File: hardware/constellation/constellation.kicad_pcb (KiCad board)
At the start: 2 copper layers, 395.2 x 272.1 mm, 122 parts

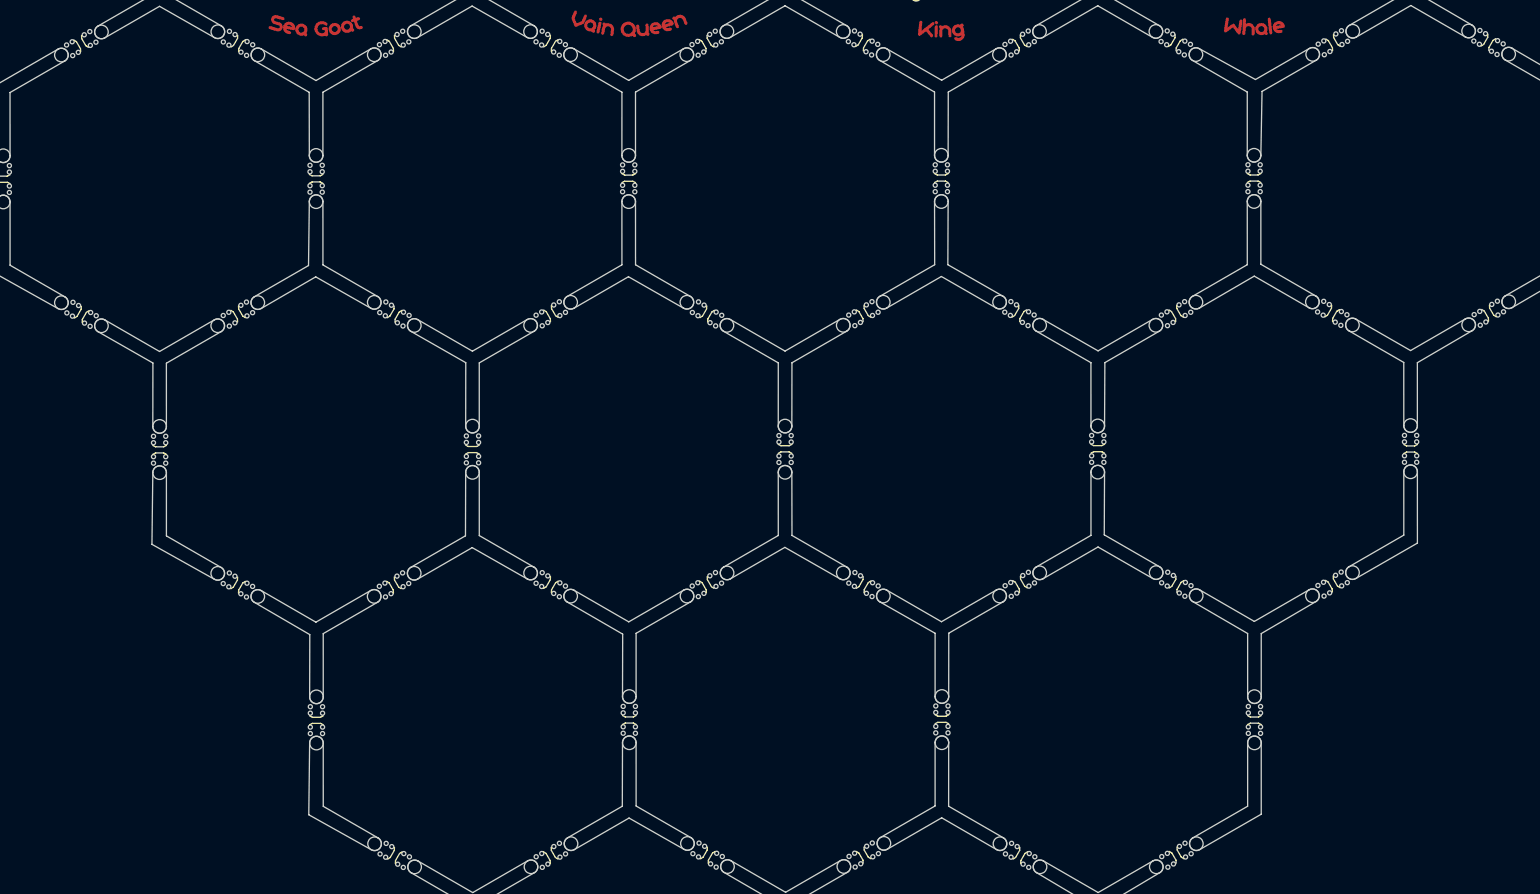
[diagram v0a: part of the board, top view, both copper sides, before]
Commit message: Added the rest of the constellations
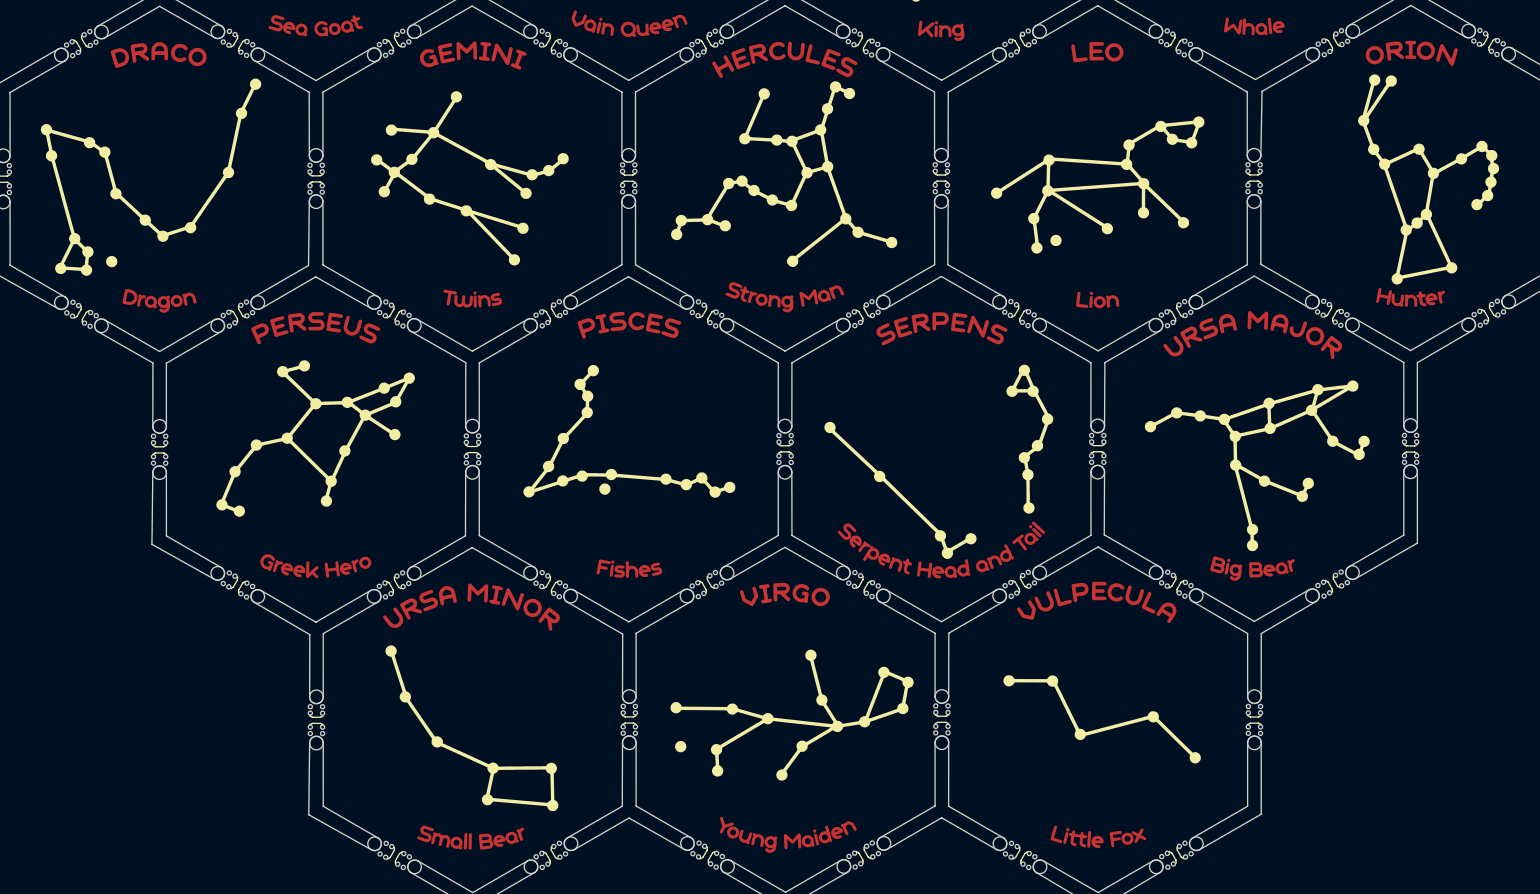
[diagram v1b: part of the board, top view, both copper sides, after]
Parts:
- added ? (x4): , Graphics, F.Cu at (143.2, 157.4)
- added ?: , Graphics, B.Cu at (51.0, 157.3)
- added ?: , Graphics, B.Cu at (120.1, 117.6)
- added ?: , Graphics, B.Cu at (74.1, 117.5)
- added ?: , Graphics, B.Cu at (189.2, 157.3)
- added ?: , Graphics, B.Cu at (74.1, 197.3)
- added ?: , Graphics, B.Cu at (143.1, 157.3)
- added ?: , Graphics, B.Cu at (97.1, 157.4)
- added ? (x4): , Graphics, F.Cu at (74.1, 117.5)
- added ? (x3): , Graphics, F.Cu at (120.2, 197.2)
- added ? (x4): , Graphics, F.Cu at (189.1, 157.2)
- added ? (x4): , Graphics, F.Cu at (120.1, 117.6)
- added ? (x4): , Graphics, F.Cu at (166.2, 197.1)
- added ? (x4): , Graphics, F.Cu at (166.1, 117.6)
- added ? (x4): , Graphics, F.Cu at (51.0, 157.3)
- added ? (x4): , Graphics, F.Cu at (212.3, 117.4)
- added ? (x4): , Graphics, F.Cu at (74.1, 197.3)
- added ? (x3): , Graphics, F.Cu at (97.2, 157.3)
- added ?: , Graphics, F.Cu at (189.2, 157.3)
- added ? (x4): , Graphics, F.Cu at (28.1, 117.6)
- added ?: , Graphics, F.Cu at (143.2, 157.3)
- added ?: , Graphics, F.Cu at (143.1, 157.3)
- added ?: , Graphics, F.Cu at (97.1, 157.4)
- added ?: , Graphics, B.Cu at (166.2, 197.1)
- added ?: , Graphics, B.Cu at (28.1, 117.6)
- added ?: , Graphics, B.Cu at (212.3, 117.4)
- added ?: , Graphics, B.Cu at (189.1, 157.2)
- added ?: , Graphics, B.Cu at (166.1, 117.6)
- added ?: , Graphics, B.Cu at (143.2, 157.3)
- added ?: , Graphics, B.Cu at (143.2, 157.4)

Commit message: Added order number and tooling holes
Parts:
- removed the mouse-bite-2mm-slot at (202.3, 246.5)
- removed the mouse-bite-2mm-slot at (110.2, 246.6)
- removed the mouse-bite-2mm-slot at (52.7, 107.3)
- removed the mouse-bite-2mm-slot at (41.2, 167.0)
- removed the mouse-bite-2mm-slot at (29.6, 147.1)
- removed the mouse-bite-2mm-slot at (236.8, 107.0)
- removed the mouse-bite-2mm-slot at (213.8, 226.7)
- removed the mouse-bite-2mm-slot at (64.1, 87.3)
- removed the mouse-bite-2mm-slot at (248.1, 126.9)
- removed the mouse-bite-2mm-slot at (52.6, 187.0)
- removed the mouse-bite-2mm-slot at (156.2, 246.6)
- removed the mouse-bite-2mm-slot at (87.3, 246.6)
- removed the mouse-bite-2mm-slot at (236.7, 186.8)
- removed the mouse-bite-2mm-slot at (110.1, 47.3)
- removed the mouse-bite-2mm-slot at (248.3, 166.8)
- removed the mouse-bite-2mm-slot at (75.7, 226.8)
- removed the mouse-bite-2mm-slot at (87.1, 47.5)
- removed the mouse-bite-2mm-slot at (133.3, 246.6)
- removed the mouse-bite-2mm-slot at (259.7, 146.8)
- removed the mouse-bite-2mm-slot at (133.2, 47.4)
- removed the mouse-bite-2mm-slot at (202.2, 47.3)
- removed the mouse-bite-2mm-slot at (225.2, 87.1)
- removed the mouse-bite-2mm-slot at (179.3, 47.3)
- removed the mouse-bite-2mm-slot at (41.0, 127.2)
- removed the mouse-bite-2mm-slot at (64.2, 206.8)
- removed the mouse-bite-2mm-slot at (225.3, 206.6)
- removed the mouse-bite-2mm-slot at (156.1, 47.3)
- removed the mouse-bite-2mm-slot at (179.3, 246.6)
- removed the mouse-bite-2mm-slot at (213.8, 67.2)
- removed the mouse-bite-2mm-slot at (75.7, 67.4)
- added REF**: Fiducial_1mm_Mask2mm, Fiducial:Fiducial_1mm_Mask2mm, F.Cu at (5.00, 20.0)
- added REF**: Fiducial_1mm_Mask2mm, Fiducial:Fiducial_1mm_Mask2mm, F.Cu at (237.0, 204.0)
- added REF**: MountingHole_2mm, MountingHole:MountingHole_2mm, F.Cu at (237.0, 5.00)
- added REF**: MountingHole_2mm, MountingHole:MountingHole_2mm, F.Cu at (237.0, 219.0)
- added REF**: MountingHole_2mm, MountingHole:MountingHole_2mm, F.Cu at (5.00, 219.0)
- added REF**: Fiducial_1mm_Mask2mm, Fiducial:Fiducial_1mm_Mask2mm, F.Cu at (222.0, 5.00)
- added REF**: Fiducial_1mm_Mask2mm, Fiducial:Fiducial_1mm_Mask2mm, F.Cu at (20.0, 219.0)
- added REF**: MountingHole_2mm, MountingHole:MountingHole_2mm, F.Cu at (5.00, 5.00)
- added mouse-bite-2mm-slot: VAL**, SWS-Library:mouse-bite-2mm-slot_edge, F.Cu at (40.5, 52.6)
- added mouse-bite-2mm-slot: VAL**, SWS-Library:mouse-bite-2mm-slot_edge, F.Cu at (155.8, 212.0)
- added mouse-bite-2mm-slot: VAL**, SWS-Library:mouse-bite-2mm-slot_edge, F.Cu at (201.6, 52.5)
- added mouse-bite-2mm-slot: VAL**, SWS-Library:mouse-bite-2mm-slot_edge, F.Cu at (86.5, 12.7)
- added mouse-bite-2mm-slot: VAL**, SWS-Library:mouse-bite-2mm-slot_edge, F.Cu at (29.1, 152.3)
- added mouse-bite-2mm-slot: VAL**, SWS-Library:mouse-bite-2mm-slot_edge, F.Cu at (224.6, 92.3)
- added mouse-bite-2mm-slot: VAL**, SWS-Library:mouse-bite-2mm-slot_edge, F.Cu at (29.1, 72.6)
- added mouse-bite-2mm-slot: VAL**, SWS-Library:mouse-bite-2mm-slot_edge, F.Cu at (52.2, 192.1)
- added mouse-bite-2mm-slot: VAL**, SWS-Library:mouse-bite-2mm-slot_edge, F.Cu at (190.2, 191.8)
- added mouse-bite-2mm-slot: VAL**, SWS-Library:mouse-bite-2mm-slot_edge, F.Cu at (86.8, 211.9)
- added mouse-bite-2mm-slot: VAL**, SWS-Library:mouse-bite-2mm-slot_edge, F.Cu at (40.7, 172.2)
- added mouse-bite-2mm-slot: VAL**, SWS-Library:mouse-bite-2mm-slot_edge, F.Cu at (201.8, 172.0)
- added mouse-bite-2mm-slot: VAL**, SWS-Library:mouse-bite-2mm-slot_edge, F.Cu at (213.2, 152.0)
- added mouse-bite-2mm-slot: VAL**, SWS-Library:mouse-bite-2mm-slot_edge, F.Cu at (109.8, 211.9)
- added mouse-bite-2mm-slot: VAL**, SWS-Library:mouse-bite-2mm-slot_edge, F.Cu at (155.6, 12.8)
- added mouse-bite-2mm-slot: VAL**, SWS-Library:mouse-bite-2mm-slot_edge, F.Cu at (63.5, 12.8)
- added mouse-bite-2mm-slot: VAL**, SWS-Library:mouse-bite-2mm-slot_edge, F.Cu at (52.1, 32.6)
- added mouse-bite-2mm-slot: VAL**, SWS-Library:mouse-bite-2mm-slot_edge, F.Cu at (17.7, 132.4)
- added mouse-bite-2mm-slot: VAL**, SWS-Library:mouse-bite-2mm-slot_edge, F.Cu at (224.8, 132.1)
- added mouse-bite-2mm-slot: VAL**, SWS-Library:mouse-bite-2mm-slot_edge, F.Cu at (109.5, 12.8)
- added mouse-bite-2mm-slot: VAL**, SWS-Library:mouse-bite-2mm-slot_edge, F.Cu at (178.8, 211.9)
- added mouse-bite-2mm-slot: VAL**, SWS-Library:mouse-bite-2mm-slot_edge, F.Cu at (63.8, 212.0)
- added mouse-bite-2mm-slot: VAL**, SWS-Library:mouse-bite-2mm-slot_edge, F.Cu at (213.3, 72.3)
- added mouse-bite-2mm-slot: VAL**, SWS-Library:mouse-bite-2mm-slot_edge, F.Cu at (178.6, 12.6)
- added mouse-bite-2mm-slot: VAL**, SWS-Library:mouse-bite-2mm-slot_edge, F.Cu at (132.6, 12.7)
- added mouse-bite-2mm-slot: VAL**, SWS-Library:mouse-bite-2mm-slot_edge, F.Cu at (17.5, 92.5)
- added mouse-bite-2mm-slot: VAL**, SWS-Library:mouse-bite-2mm-slot_edge, F.Cu at (132.8, 211.8)
- added mouse-bite-2mm-slot: VAL**, SWS-Library:mouse-bite-2mm-slot_edge, F.Cu at (190.2, 32.5)
- moved ? 41.9 mm to (73.6, 43.0) (x5)
- moved mouse-bite-2mm-slot 41.9 mm to (86.7, 92.5)
- moved mouse-bite-2mm-slot 41.9 mm to (155.6, 52.5)
- moved ? 41.9 mm to (27.5, 43.0) (x5)
- moved mouse-bite-2mm-slot 41.9 mm to (109.6, 52.5)
- moved mouse-bite-2mm-slot 41.9 mm to (132.8, 172.1)
- moved ? 41.9 mm to (142.7, 162.4)
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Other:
- board size 395.2 x 272.1 mm -> 242 x 224 mm
- board text added: "JLCJLCJLCJLC"

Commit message: Roughly placed all the LEDs
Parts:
- added TP266: TestPoint, TestPoint:TestPoint_Pad_D1.5mm, F.Cu at (2.58, 25.7)
- added TP267: TestPoint, TestPoint:TestPoint_Pad_D1.5mm, F.Cu at (2.41, 29.8)
- added TP268: TestPoint, TestPoint:TestPoint_Pad_D1.5mm, F.Cu at (2.41, 33.3)
- added U1: XL-1010RGBC, easyeda2kicad:LED-SMD_4P-L1.0-W1.0-TL_XL-1010RGBC-WS2812B, F.Cu at (65.5, 21.0)
- added U10: XL-1010RGBC, easyeda2kicad:LED-SMD_4P-L1.0-W1.0-TL_XL-1010RGBC-WS2812B, F.Cu at (74.1, 40.8)
- added U100: XL-1010RGBC, easyeda2kicad:LED-SMD_4P-L1.0-W1.0-TL_XL-1010RGBC-WS2812B, F.Cu at (22.1, 124.6)
- added U101: XL-1010RGBC, easyeda2kicad:LED-SMD_4P-L1.0-W1.0-TL_XL-1010RGBC-WS2812B, F.Cu at (61.1, 109.6)
- added U102: XL-1010RGBC, easyeda2kicad:LED-SMD_4P-L1.0-W1.0-TL_XL-1010RGBC-WS2812B, F.Cu at (62.2, 114.3)
- added U103: XL-1010RGBC, easyeda2kicad:LED-SMD_4P-L1.0-W1.0-TL_XL-1010RGBC-WS2812B, F.Cu at (63.6, 111.4)
- added U104: XL-1010RGBC, easyeda2kicad:LED-SMD_4P-L1.0-W1.0-TL_XL-1010RGBC-WS2812B, F.Cu at (66.2, 109.5)
- added U105: XL-1010RGBC, easyeda2kicad:LED-SMD_4P-L1.0-W1.0-TL_XL-1010RGBC-WS2812B, F.Cu at (68.9, 115.4)
- added U106: XL-1010RGBC, easyeda2kicad:LED-SMD_4P-L1.0-W1.0-TL_XL-1010RGBC-WS2812B, F.Cu at (74.2, 117.1)
- added U107: XL-1010RGBC, easyeda2kicad:LED-SMD_4P-L1.0-W1.0-TL_XL-1010RGBC-WS2812B, F.Cu at (81.3, 124.3)
- added U108: XL-1010RGBC, easyeda2kicad:LED-SMD_4P-L1.0-W1.0-TL_XL-1010RGBC-WS2812B, F.Cu at (82.6, 119.7)
- added U109: XL-1010RGBC, easyeda2kicad:LED-SMD_4P-L1.0-W1.0-TL_XL-1010RGBC-WS2812B, F.Cu at (63.2, 105.1)
- added U11: XL-1010RGBC, easyeda2kicad:LED-SMD_4P-L1.0-W1.0-TL_XL-1010RGBC-WS2812B, F.Cu at (74.3, 38.5)
- added U110: XL-1010RGBC, easyeda2kicad:LED-SMD_4P-L1.0-W1.0-TL_XL-1010RGBC-WS2812B, F.Cu at (69.4, 105.6)
- added U111: XL-1010RGBC, easyeda2kicad:LED-SMD_4P-L1.0-W1.0-TL_XL-1010RGBC-WS2812B, F.Cu at (72.8, 100.3)
- added U112: XL-1010RGBC, easyeda2kicad:LED-SMD_4P-L1.0-W1.0-TL_XL-1010RGBC-WS2812B, F.Cu at (77.8, 110.3)
- added U113: XL-1010RGBC, easyeda2kicad:LED-SMD_4P-L1.0-W1.0-TL_XL-1010RGBC-WS2812B, F.Cu at (83.1, 114.5)
- added U114: XL-1010RGBC, easyeda2kicad:LED-SMD_4P-L1.0-W1.0-TL_XL-1010RGBC-WS2812B, F.Cu at (83.9, 111.8)
- added U115: XL-1010RGBC, easyeda2kicad:LED-SMD_4P-L1.0-W1.0-TL_XL-1010RGBC-WS2812B, F.Cu at (86.3, 111.2)
- added U116: XL-1010RGBC, easyeda2kicad:LED-SMD_4P-L1.0-W1.0-TL_XL-1010RGBC-WS2812B, F.Cu at (88.5, 109.4)
- added U117: XL-1010RGBC, easyeda2kicad:LED-SMD_4P-L1.0-W1.0-TL_XL-1010RGBC-WS2812B, F.Cu at (105.2, 120.6)
- added U118: XL-1010RGBC, easyeda2kicad:LED-SMD_4P-L1.0-W1.0-TL_XL-1010RGBC-WS2812B, F.Cu at (105.9, 118.4)
- added U119: XL-1010RGBC, easyeda2kicad:LED-SMD_4P-L1.0-W1.0-TL_XL-1010RGBC-WS2812B, F.Cu at (109.7, 118.4)
- added U12: XL-1010RGBC, easyeda2kicad:LED-SMD_4P-L1.0-W1.0-TL_XL-1010RGBC-WS2812B, F.Cu at (74.6, 36.1)
- added U120: XL-1010RGBC, easyeda2kicad:LED-SMD_4P-L1.0-W1.0-TL_XL-1010RGBC-WS2812B, F.Cu at (112.4, 119.3)
- added U121: XL-1010RGBC, easyeda2kicad:LED-SMD_4P-L1.0-W1.0-TL_XL-1010RGBC-WS2812B, F.Cu at (112.8, 113.1)
- added U122: XL-1010RGBC, easyeda2kicad:LED-SMD_4P-L1.0-W1.0-TL_XL-1010RGBC-WS2812B, F.Cu at (114.9, 112.7)
- added U123: XL-1010RGBC, easyeda2kicad:LED-SMD_4P-L1.0-W1.0-TL_XL-1010RGBC-WS2812B, F.Cu at (116.6, 114.1)
- added U124: XL-1010RGBC, easyeda2kicad:LED-SMD_4P-L1.0-W1.0-TL_XL-1010RGBC-WS2812B, F.Cu at (119.3, 115.5)
- added U125: XL-1010RGBC, easyeda2kicad:LED-SMD_4P-L1.0-W1.0-TL_XL-1010RGBC-WS2812B, F.Cu at (122.1, 116.3)
- added U126: XL-1010RGBC, easyeda2kicad:LED-SMD_4P-L1.0-W1.0-TL_XL-1010RGBC-WS2812B, F.Cu at (124.4, 111.5)
- added U127: XL-1010RGBC, easyeda2kicad:LED-SMD_4P-L1.0-W1.0-TL_XL-1010RGBC-WS2812B, F.Cu at (122.2, 106.8)
- added U128: XL-1010RGBC, easyeda2kicad:LED-SMD_4P-L1.0-W1.0-TL_XL-1010RGBC-WS2812B, F.Cu at (119.9, 106.7)
- added U129: XL-1010RGBC, easyeda2kicad:LED-SMD_4P-L1.0-W1.0-TL_XL-1010RGBC-WS2812B, F.Cu at (115.2, 106.5)
- added U13: XL-1010RGBC, easyeda2kicad:LED-SMD_4P-L1.0-W1.0-TL_XL-1010RGBC-WS2812B, F.Cu at (78.5, 33.6)
- added U130: XL-1010RGBC, easyeda2kicad:LED-SMD_4P-L1.0-W1.0-TL_XL-1010RGBC-WS2812B, F.Cu at (118.1, 99.9)
- added U131: XL-1010RGBC, easyeda2kicad:LED-SMD_4P-L1.0-W1.0-TL_XL-1010RGBC-WS2812B, F.Cu at (130.7, 99.8)
- added U132: XL-1010RGBC, easyeda2kicad:LED-SMD_4P-L1.0-W1.0-TL_XL-1010RGBC-WS2812B, F.Cu at (128.6, 98.9)
- added U133: XL-1010RGBC, easyeda2kicad:LED-SMD_4P-L1.0-W1.0-TL_XL-1010RGBC-WS2812B, F.Cu at (127.4, 102.1)
- added U134: XL-1010RGBC, easyeda2kicad:LED-SMD_4P-L1.0-W1.0-TL_XL-1010RGBC-WS2812B, F.Cu at (126.4, 105.2)
- added U135: XL-1010RGBC, easyeda2kicad:LED-SMD_4P-L1.0-W1.0-TL_XL-1010RGBC-WS2812B, F.Cu at (127.3, 110.6)
- added U136: XL-1010RGBC, easyeda2kicad:LED-SMD_4P-L1.0-W1.0-TL_XL-1010RGBC-WS2812B, F.Cu at (130.1, 118.2)
- added U137: XL-1010RGBC, easyeda2kicad:LED-SMD_4P-L1.0-W1.0-TL_XL-1010RGBC-WS2812B, F.Cu at (122.3, 124.5)
- added U138: XL-1010RGBC, easyeda2kicad:LED-SMD_4P-L1.0-W1.0-TL_XL-1010RGBC-WS2812B, F.Cu at (131.9, 120.2)
- added U139: XL-1010RGBC, easyeda2kicad:LED-SMD_4P-L1.0-W1.0-TL_XL-1010RGBC-WS2812B, F.Cu at (136.8, 121.8)
- added U14: XL-1010RGBC, easyeda2kicad:LED-SMD_4P-L1.0-W1.0-TL_XL-1010RGBC-WS2812B, F.Cu at (78.6, 31.1)
- added U140: XL-1010RGBC, easyeda2kicad:LED-SMD_4P-L1.0-W1.0-TL_XL-1010RGBC-WS2812B, F.Cu at (152.3, 114.5)
- added U141: XL-1010RGBC, easyeda2kicad:LED-SMD_4P-L1.0-W1.0-TL_XL-1010RGBC-WS2812B, F.Cu at (160.0, 109.6)
- added U142: XL-1010RGBC, easyeda2kicad:LED-SMD_4P-L1.0-W1.0-TL_XL-1010RGBC-WS2812B, F.Cu at (159.8, 114.2)
- added U143: XL-1010RGBC, easyeda2kicad:LED-SMD_4P-L1.0-W1.0-TL_XL-1010RGBC-WS2812B, F.Cu at (157.8, 118.3)
- added U144: XL-1010RGBC, easyeda2kicad:LED-SMD_4P-L1.0-W1.0-TL_XL-1010RGBC-WS2812B, F.Cu at (158.2, 122.6)
- added U145: XL-1010RGBC, easyeda2kicad:LED-SMD_4P-L1.0-W1.0-TL_XL-1010RGBC-WS2812B, F.Cu at (161.0, 121.5)
- added U146: XL-1010RGBC, easyeda2kicad:LED-SMD_4P-L1.0-W1.0-TL_XL-1010RGBC-WS2812B, F.Cu at (168.6, 119.7)
- added U147: XL-1010RGBC, easyeda2kicad:LED-SMD_4P-L1.0-W1.0-TL_XL-1010RGBC-WS2812B, F.Cu at (173.9, 117.4)
- added U148: XL-1010RGBC, easyeda2kicad:LED-SMD_4P-L1.0-W1.0-TL_XL-1010RGBC-WS2812B, F.Cu at (179.8, 118.9)
- added U149: XL-1010RGBC, easyeda2kicad:LED-SMD_4P-L1.0-W1.0-TL_XL-1010RGBC-WS2812B, F.Cu at (173.9, 113.1)
- added U15: XL-1010RGBC, easyeda2kicad:LED-SMD_4P-L1.0-W1.0-TL_XL-1010RGBC-WS2812B, F.Cu at (84.7, 25.7)
- added U150: XL-1010RGBC, easyeda2kicad:LED-SMD_4P-L1.0-W1.0-TL_XL-1010RGBC-WS2812B, F.Cu at (171.4, 110.2)
- added U151: XL-1010RGBC, easyeda2kicad:LED-SMD_4P-L1.0-W1.0-TL_XL-1010RGBC-WS2812B, F.Cu at (171.7, 107.4)
- added U152: XL-1010RGBC, easyeda2kicad:LED-SMD_4P-L1.0-W1.0-TL_XL-1010RGBC-WS2812B, F.Cu at (176.4, 104.7)
- added U153: XL-1010RGBC, easyeda2kicad:LED-SMD_4P-L1.0-W1.0-TL_XL-1010RGBC-WS2812B, F.Cu at (178.1, 106.6)
- added U154: XL-1010RGBC, easyeda2kicad:LED-SMD_4P-L1.0-W1.0-TL_XL-1010RGBC-WS2812B, F.Cu at (181.0, 107.1)
- added U155: XL-1010RGBC, easyeda2kicad:LED-SMD_4P-L1.0-W1.0-TL_XL-1010RGBC-WS2812B, F.Cu at (182.0, 104.0)
- added U156: XL-1010RGBC, easyeda2kicad:LED-SMD_4P-L1.0-W1.0-TL_XL-1010RGBC-WS2812B, F.Cu at (207.9, 97.8)
- added U157: XL-1010RGBC, easyeda2kicad:LED-SMD_4P-L1.0-W1.0-TL_XL-1010RGBC-WS2812B, F.Cu at (210.4, 98.0)
- added U158: XL-1010RGBC, easyeda2kicad:LED-SMD_4P-L1.0-W1.0-TL_XL-1010RGBC-WS2812B, F.Cu at (206.3, 103.8)
- added U159: XL-1010RGBC, easyeda2kicad:LED-SMD_4P-L1.0-W1.0-TL_XL-1010RGBC-WS2812B, F.Cu at (207.8, 108.0)
- added U16: XL-1010RGBC, easyeda2kicad:LED-SMD_4P-L1.0-W1.0-TL_XL-1010RGBC-WS2812B, F.Cu at (91.5, 26.6)
- added U160: XL-1010RGBC, easyeda2kicad:LED-SMD_4P-L1.0-W1.0-TL_XL-1010RGBC-WS2812B, F.Cu at (209.4, 110.2)
- added U161: XL-1010RGBC, easyeda2kicad:LED-SMD_4P-L1.0-W1.0-TL_XL-1010RGBC-WS2812B, F.Cu at (212.5, 119.9)
- added U162: XL-1010RGBC, easyeda2kicad:LED-SMD_4P-L1.0-W1.0-TL_XL-1010RGBC-WS2812B, F.Cu at (214.2, 118.8)
- added U163: XL-1010RGBC, easyeda2kicad:LED-SMD_4P-L1.0-W1.0-TL_XL-1010RGBC-WS2812B, F.Cu at (215.7, 117.5)
- added U164: XL-1010RGBC, easyeda2kicad:LED-SMD_4P-L1.0-W1.0-TL_XL-1010RGBC-WS2812B, F.Cu at (216.5, 111.5)
- added U165: XL-1010RGBC, easyeda2kicad:LED-SMD_4P-L1.0-W1.0-TL_XL-1010RGBC-WS2812B, F.Cu at (214.4, 108.0)
- added U166: XL-1010RGBC, easyeda2kicad:LED-SMD_4P-L1.0-W1.0-TL_XL-1010RGBC-WS2812B, F.Cu at (220.7, 109.4)
- added U167: XL-1010RGBC, easyeda2kicad:LED-SMD_4P-L1.0-W1.0-TL_XL-1010RGBC-WS2812B, F.Cu at (223.6, 107.5)
- added U168: XL-1010RGBC, easyeda2kicad:LED-SMD_4P-L1.0-W1.0-TL_XL-1010RGBC-WS2812B, F.Cu at (225.4, 108.8)
- added U169: XL-1010RGBC, easyeda2kicad:LED-SMD_4P-L1.0-W1.0-TL_XL-1010RGBC-WS2812B, F.Cu at (225.5, 110.9)
- added U17: XL-1010RGBC, easyeda2kicad:LED-SMD_4P-L1.0-W1.0-TL_XL-1010RGBC-WS2812B, F.Cu at (80.6, 40.7)
- added U170: XL-1010RGBC, easyeda2kicad:LED-SMD_4P-L1.0-W1.0-TL_XL-1010RGBC-WS2812B, F.Cu at (225.1, 112.9)
- added U171: XL-1010RGBC, easyeda2kicad:LED-SMD_4P-L1.0-W1.0-TL_XL-1010RGBC-WS2812B, F.Cu at (224.6, 114.9)
- added U172: XL-1010RGBC, easyeda2kicad:LED-SMD_4P-L1.0-W1.0-TL_XL-1010RGBC-WS2812B, F.Cu at (222.8, 116.3)
- added U173: XL-1010RGBC, easyeda2kicad:LED-SMD_4P-L1.0-W1.0-TL_XL-1010RGBC-WS2812B, F.Cu at (219.3, 125.5)
- added U174: XL-1010RGBC, easyeda2kicad:LED-SMD_4P-L1.0-W1.0-TL_XL-1010RGBC-WS2812B, F.Cu at (211.2, 127.1)
- added U175: XL-1010RGBC, easyeda2kicad:LED-SMD_4P-L1.0-W1.0-TL_XL-1010RGBC-WS2812B, F.Cu at (204.7, 142.9)
- added U176: XL-1010RGBC, easyeda2kicad:LED-SMD_4P-L1.0-W1.0-TL_XL-1010RGBC-WS2812B, F.Cu at (199.5, 143.5)
- added U177: XL-1010RGBC, easyeda2kicad:LED-SMD_4P-L1.0-W1.0-TL_XL-1010RGBC-WS2812B, F.Cu at (192.4, 145.4)
- added U178: XL-1010RGBC, easyeda2kicad:LED-SMD_4P-L1.0-W1.0-TL_XL-1010RGBC-WS2812B, F.Cu at (185.8, 147.8)
- added U179: XL-1010RGBC, easyeda2kicad:LED-SMD_4P-L1.0-W1.0-TL_XL-1010RGBC-WS2812B, F.Cu at (187.4, 150.3)
- added U18: XL-1010RGBC, easyeda2kicad:LED-SMD_4P-L1.0-W1.0-TL_XL-1010RGBC-WS2812B, F.Cu at (107.4, 37.4)
- added U180: XL-1010RGBC, easyeda2kicad:LED-SMD_4P-L1.0-W1.0-TL_XL-1010RGBC-WS2812B, F.Cu at (192.5, 149.1)
- added U181: XL-1010RGBC, easyeda2kicad:LED-SMD_4P-L1.0-W1.0-TL_XL-1010RGBC-WS2812B, F.Cu at (198.7, 146.5)
- added U182: XL-1010RGBC, easyeda2kicad:LED-SMD_4P-L1.0-W1.0-TL_XL-1010RGBC-WS2812B, F.Cu at (201.8, 151.0)
- added U183: XL-1010RGBC, easyeda2kicad:LED-SMD_4P-L1.0-W1.0-TL_XL-1010RGBC-WS2812B, F.Cu at (205.6, 153.0)
- added U184: XL-1010RGBC, easyeda2kicad:LED-SMD_4P-L1.0-W1.0-TL_XL-1010RGBC-WS2812B, F.Cu at (206.4, 151.0)
- added U185: XL-1010RGBC, easyeda2kicad:LED-SMD_4P-L1.0-W1.0-TL_XL-1010RGBC-WS2812B, F.Cu at (198.1, 157.3)
- added U186: XL-1010RGBC, easyeda2kicad:LED-SMD_4P-L1.0-W1.0-TL_XL-1010RGBC-WS2812B, F.Cu at (197.3, 159.2)
- added U187: XL-1010RGBC, easyeda2kicad:LED-SMD_4P-L1.0-W1.0-TL_XL-1010RGBC-WS2812B, F.Cu at (191.7, 156.9)
- added U188: XL-1010RGBC, easyeda2kicad:LED-SMD_4P-L1.0-W1.0-TL_XL-1010RGBC-WS2812B, F.Cu at (190.0, 166.4)
- added U189: XL-1010RGBC, easyeda2kicad:LED-SMD_4P-L1.0-W1.0-TL_XL-1010RGBC-WS2812B, F.Cu at (189.9, 164.0)
- added U19: XL-1010RGBC, easyeda2kicad:LED-SMD_4P-L1.0-W1.0-TL_XL-1010RGBC-WS2812B, F.Cu at (111.8, 30.8)
- added U190: XL-1010RGBC, easyeda2kicad:LED-SMD_4P-L1.0-W1.0-TL_XL-1010RGBC-WS2812B, F.Cu at (187.4, 154.5)
- added U191: XL-1010RGBC, easyeda2kicad:LED-SMD_4P-L1.0-W1.0-TL_XL-1010RGBC-WS2812B, F.Cu at (182.2, 147.3)
- added U192: XL-1010RGBC, easyeda2kicad:LED-SMD_4P-L1.0-W1.0-TL_XL-1010RGBC-WS2812B, F.Cu at (178.8, 146.9)
- added U193: XL-1010RGBC, easyeda2kicad:LED-SMD_4P-L1.0-W1.0-TL_XL-1010RGBC-WS2812B, F.Cu at (174.9, 148.8)
- added U194: XL-1010RGBC, easyeda2kicad:LED-SMD_4P-L1.0-W1.0-TL_XL-1010RGBC-WS2812B, F.Cu at (156.3, 140.5)
- added U195: XL-1010RGBC, easyeda2kicad:LED-SMD_4P-L1.0-W1.0-TL_XL-1010RGBC-WS2812B, F.Cu at (154.6, 143.7)
- added U196: XL-1010RGBC, easyeda2kicad:LED-SMD_4P-L1.0-W1.0-TL_XL-1010RGBC-WS2812B, F.Cu at (157.7, 143.7)
- added U197: XL-1010RGBC, easyeda2kicad:LED-SMD_4P-L1.0-W1.0-TL_XL-1010RGBC-WS2812B, F.Cu at (159.8, 147.8)
- added U198: XL-1010RGBC, easyeda2kicad:LED-SMD_4P-L1.0-W1.0-TL_XL-1010RGBC-WS2812B, F.Cu at (158.4, 151.6)
- added U199: XL-1010RGBC, easyeda2kicad:LED-SMD_4P-L1.0-W1.0-TL_XL-1010RGBC-WS2812B, F.Cu at (156.4, 153.4)
- added U2: XL-1010RGBC, easyeda2kicad:LED-SMD_4P-L1.0-W1.0-TL_XL-1010RGBC-WS2812B, F.Cu at (70.0, 23.0)
- added U20: XL-1010RGBC, easyeda2kicad:LED-SMD_4P-L1.0-W1.0-TL_XL-1010RGBC-WS2812B, F.Cu at (115.9, 31.6)
- added U200: XL-1010RGBC, easyeda2kicad:LED-SMD_4P-L1.0-W1.0-TL_XL-1010RGBC-WS2812B, F.Cu at (156.9, 155.9)
- added U201: XL-1010RGBC, easyeda2kicad:LED-SMD_4P-L1.0-W1.0-TL_XL-1010RGBC-WS2812B, F.Cu at (157.0, 160.8)
- added U202: XL-1010RGBC, easyeda2kicad:LED-SMD_4P-L1.0-W1.0-TL_XL-1010RGBC-WS2812B, F.Cu at (148.6, 165.3)
- added U203: XL-1010RGBC, easyeda2kicad:LED-SMD_4P-L1.0-W1.0-TL_XL-1010RGBC-WS2812B, F.Cu at (145.0, 167.6)
- added U204: XL-1010RGBC, easyeda2kicad:LED-SMD_4P-L1.0-W1.0-TL_XL-1010RGBC-WS2812B, F.Cu at (144.0, 164.9)
- added U205: XL-1010RGBC, easyeda2kicad:LED-SMD_4P-L1.0-W1.0-TL_XL-1010RGBC-WS2812B, F.Cu at (135.0, 156.1)
- added U206: XL-1010RGBC, easyeda2kicad:LED-SMD_4P-L1.0-W1.0-TL_XL-1010RGBC-WS2812B, F.Cu at (127.8, 148.9)
- added U207: XL-1010RGBC, easyeda2kicad:LED-SMD_4P-L1.0-W1.0-TL_XL-1010RGBC-WS2812B, F.Cu at (113.0, 157.8)
- added U208: XL-1010RGBC, easyeda2kicad:LED-SMD_4P-L1.0-W1.0-TL_XL-1010RGBC-WS2812B, F.Cu at (110.9, 158.4)
- added U209: XL-1010RGBC, easyeda2kicad:LED-SMD_4P-L1.0-W1.0-TL_XL-1010RGBC-WS2812B, F.Cu at (108.9, 156.4)
- added U21: XL-1010RGBC, easyeda2kicad:LED-SMD_4P-L1.0-W1.0-TL_XL-1010RGBC-WS2812B, F.Cu at (116.1, 36.6)
- added U210: XL-1010RGBC, easyeda2kicad:LED-SMD_4P-L1.0-W1.0-TL_XL-1010RGBC-WS2812B, F.Cu at (106.6, 157.4)
- added U211: XL-1010RGBC, easyeda2kicad:LED-SMD_4P-L1.0-W1.0-TL_XL-1010RGBC-WS2812B, F.Cu at (103.7, 156.6)
- added U212: XL-1010RGBC, easyeda2kicad:LED-SMD_4P-L1.0-W1.0-TL_XL-1010RGBC-WS2812B, F.Cu at (95.6, 155.9)
- added U213: XL-1010RGBC, easyeda2kicad:LED-SMD_4P-L1.0-W1.0-TL_XL-1010RGBC-WS2812B, F.Cu at (94.6, 158.1)
- added U214: XL-1010RGBC, easyeda2kicad:LED-SMD_4P-L1.0-W1.0-TL_XL-1010RGBC-WS2812B, F.Cu at (91.2, 156.1)
- added U215: XL-1010RGBC, easyeda2kicad:LED-SMD_4P-L1.0-W1.0-TL_XL-1010RGBC-WS2812B, F.Cu at (88.4, 156.8)
- added U216: XL-1010RGBC, easyeda2kicad:LED-SMD_4P-L1.0-W1.0-TL_XL-1010RGBC-WS2812B, F.Cu at (83.4, 158.4)
- added U217: XL-1010RGBC, easyeda2kicad:LED-SMD_4P-L1.0-W1.0-TL_XL-1010RGBC-WS2812B, F.Cu at (86.3, 154.7)
- added U218: XL-1010RGBC, easyeda2kicad:LED-SMD_4P-L1.0-W1.0-TL_XL-1010RGBC-WS2812B, F.Cu at (88.5, 150.6)
- added U219: XL-1010RGBC, easyeda2kicad:LED-SMD_4P-L1.0-W1.0-TL_XL-1010RGBC-WS2812B, F.Cu at (92.0, 146.8)
- added U22: XL-1010RGBC, easyeda2kicad:LED-SMD_4P-L1.0-W1.0-TL_XL-1010RGBC-WS2812B, F.Cu at (115.4, 39.3)
- added U220: XL-1010RGBC, easyeda2kicad:LED-SMD_4P-L1.0-W1.0-TL_XL-1010RGBC-WS2812B, F.Cu at (92.1, 144.4)
- added U221: XL-1010RGBC, easyeda2kicad:LED-SMD_4P-L1.0-W1.0-TL_XL-1010RGBC-WS2812B, F.Cu at (91.0, 142.6)
- added U222: XL-1010RGBC, easyeda2kicad:LED-SMD_4P-L1.0-W1.0-TL_XL-1010RGBC-WS2812B, F.Cu at (93.0, 140.6)
- added U223: XL-1010RGBC, easyeda2kicad:LED-SMD_4P-L1.0-W1.0-TL_XL-1010RGBC-WS2812B, F.Cu at (63.8, 150.0)
- added U224: XL-1010RGBC, easyeda2kicad:LED-SMD_4P-L1.0-W1.0-TL_XL-1010RGBC-WS2812B, F.Cu at (59.4, 147.1)
- added U225: XL-1010RGBC, easyeda2kicad:LED-SMD_4P-L1.0-W1.0-TL_XL-1010RGBC-WS2812B, F.Cu at (63.9, 145.2)
- added U226: XL-1010RGBC, easyeda2kicad:LED-SMD_4P-L1.0-W1.0-TL_XL-1010RGBC-WS2812B, F.Cu at (65.9, 141.7)
- added U227: XL-1010RGBC, easyeda2kicad:LED-SMD_4P-L1.0-W1.0-TL_XL-1010RGBC-WS2812B, F.Cu at (62.2, 143.2)
- added U228: XL-1010RGBC, easyeda2kicad:LED-SMD_4P-L1.0-W1.0-TL_XL-1010RGBC-WS2812B, F.Cu at (56.7, 145.3)
- added U229: XL-1010RGBC, easyeda2kicad:LED-SMD_4P-L1.0-W1.0-TL_XL-1010RGBC-WS2812B, F.Cu at (52.1, 145.6)
- added U23: XL-1010RGBC, easyeda2kicad:LED-SMD_4P-L1.0-W1.0-TL_XL-1010RGBC-WS2812B, F.Cu at (117.2, 28.6)
- added U230: XL-1010RGBC, easyeda2kicad:LED-SMD_4P-L1.0-W1.0-TL_XL-1010RGBC-WS2812B, F.Cu at (47.2, 140.7)
- added U231: XL-1010RGBC, easyeda2kicad:LED-SMD_4P-L1.0-W1.0-TL_XL-1010RGBC-WS2812B, F.Cu at (50.5, 139.9)
- added U232: XL-1010RGBC, easyeda2kicad:LED-SMD_4P-L1.0-W1.0-TL_XL-1010RGBC-WS2812B, F.Cu at (48.2, 150.4)
- added U233: XL-1010RGBC, easyeda2kicad:LED-SMD_4P-L1.0-W1.0-TL_XL-1010RGBC-WS2812B, F.Cu at (43.3, 151.6)
- added U234: XL-1010RGBC, easyeda2kicad:LED-SMD_4P-L1.0-W1.0-TL_XL-1010RGBC-WS2812B, F.Cu at (40.3, 155.4)
- added U235: XL-1010RGBC, easyeda2kicad:LED-SMD_4P-L1.0-W1.0-TL_XL-1010RGBC-WS2812B, F.Cu at (38.4, 160.4)
- added U236: XL-1010RGBC, easyeda2kicad:LED-SMD_4P-L1.0-W1.0-TL_XL-1010RGBC-WS2812B, F.Cu at (40.9, 161.3)
- added U237: XL-1010RGBC, easyeda2kicad:LED-SMD_4P-L1.0-W1.0-TL_XL-1010RGBC-WS2812B, F.Cu at (56.3, 152.4)
- added U238: XL-1010RGBC, easyeda2kicad:LED-SMD_4P-L1.0-W1.0-TL_XL-1010RGBC-WS2812B, F.Cu at (54.3, 156.8)
- added U239: XL-1010RGBC, easyeda2kicad:LED-SMD_4P-L1.0-W1.0-TL_XL-1010RGBC-WS2812B, F.Cu at (53.7, 159.8)
- added U24: XL-1010RGBC, easyeda2kicad:LED-SMD_4P-L1.0-W1.0-TL_XL-1010RGBC-WS2812B, F.Cu at (121.2, 27.2)
- added U240: XL-1010RGBC, easyeda2kicad:LED-SMD_4P-L1.0-W1.0-TL_XL-1010RGBC-WS2812B, F.Cu at (63.2, 181.9)
- added U241: XL-1010RGBC, easyeda2kicad:LED-SMD_4P-L1.0-W1.0-TL_XL-1010RGBC-WS2812B, F.Cu at (65.4, 188.7)
- added U242: XL-1010RGBC, easyeda2kicad:LED-SMD_4P-L1.0-W1.0-TL_XL-1010RGBC-WS2812B, F.Cu at (69.9, 195.3)
- added U243: XL-1010RGBC, easyeda2kicad:LED-SMD_4P-L1.0-W1.0-TL_XL-1010RGBC-WS2812B, F.Cu at (78.2, 199.1)
- added U244: XL-1010RGBC, easyeda2kicad:LED-SMD_4P-L1.0-W1.0-TL_XL-1010RGBC-WS2812B, F.Cu at (77.4, 203.8)
- added U245: XL-1010RGBC, easyeda2kicad:LED-SMD_4P-L1.0-W1.0-TL_XL-1010RGBC-WS2812B, F.Cu at (87.1, 204.5)
- added U246: XL-1010RGBC, easyeda2kicad:LED-SMD_4P-L1.0-W1.0-TL_XL-1010RGBC-WS2812B, F.Cu at (86.7, 199.2)
- added U247: XL-1010RGBC, easyeda2kicad:LED-SMD_4P-L1.0-W1.0-TL_XL-1010RGBC-WS2812B, F.Cu at (105.1, 190.2)
- added U248: XL-1010RGBC, easyeda2kicad:LED-SMD_4P-L1.0-W1.0-TL_XL-1010RGBC-WS2812B, F.Cu at (105.8, 196.0)
- added U249: XL-1010RGBC, easyeda2kicad:LED-SMD_4P-L1.0-W1.0-TL_XL-1010RGBC-WS2812B, F.Cu at (113.4, 190.4)
- added U25: XL-1010RGBC, easyeda2kicad:LED-SMD_4P-L1.0-W1.0-TL_XL-1010RGBC-WS2812B, F.Cu at (124.2, 26.3)
- added U250: XL-1010RGBC, easyeda2kicad:LED-SMD_4P-L1.0-W1.0-TL_XL-1010RGBC-WS2812B, F.Cu at (118.6, 191.8)
- added U251: XL-1010RGBC, easyeda2kicad:LED-SMD_4P-L1.0-W1.0-TL_XL-1010RGBC-WS2812B, F.Cu at (111.0, 196.3)
- added U252: XL-1010RGBC, easyeda2kicad:LED-SMD_4P-L1.0-W1.0-TL_XL-1010RGBC-WS2812B, F.Cu at (111.1, 199.5)
- added U253: XL-1010RGBC, easyeda2kicad:LED-SMD_4P-L1.0-W1.0-TL_XL-1010RGBC-WS2812B, F.Cu at (120.8, 200.1)
- added U254: XL-1010RGBC, easyeda2kicad:LED-SMD_4P-L1.0-W1.0-TL_XL-1010RGBC-WS2812B, F.Cu at (123.6, 195.9)
- added U255: XL-1010RGBC, easyeda2kicad:LED-SMD_4P-L1.0-W1.0-TL_XL-1010RGBC-WS2812B, F.Cu at (128.9, 192.8)
- added U256: XL-1010RGBC, easyeda2kicad:LED-SMD_4P-L1.0-W1.0-TL_XL-1010RGBC-WS2812B, F.Cu at (126.5, 189.1)
- added U257: XL-1010RGBC, easyeda2kicad:LED-SMD_4P-L1.0-W1.0-TL_XL-1010RGBC-WS2812B, F.Cu at (124.9, 182.5)
- added U258: XL-1010RGBC, easyeda2kicad:LED-SMD_4P-L1.0-W1.0-TL_XL-1010RGBC-WS2812B, F.Cu at (132.8, 192.3)
- added U259: XL-1010RGBC, easyeda2kicad:LED-SMD_4P-L1.0-W1.0-TL_XL-1010RGBC-WS2812B, F.Cu at (135.7, 185.1)
- added U26: XL-1010RGBC, easyeda2kicad:LED-SMD_4P-L1.0-W1.0-TL_XL-1010RGBC-WS2812B, F.Cu at (122.2, 31.7)
- added U260: XL-1010RGBC, easyeda2kicad:LED-SMD_4P-L1.0-W1.0-TL_XL-1010RGBC-WS2812B, F.Cu at (139.2, 186.5)
- added U261: XL-1010RGBC, easyeda2kicad:LED-SMD_4P-L1.0-W1.0-TL_XL-1010RGBC-WS2812B, F.Cu at (138.5, 190.3)
- added U262: XL-1010RGBC, easyeda2kicad:LED-SMD_4P-L1.0-W1.0-TL_XL-1010RGBC-WS2812B, F.Cu at (154.1, 186.0)
- added U263: XL-1010RGBC, easyeda2kicad:LED-SMD_4P-L1.0-W1.0-TL_XL-1010RGBC-WS2812B, F.Cu at (160.5, 186.1)
- added U264: XL-1010RGBC, easyeda2kicad:LED-SMD_4P-L1.0-W1.0-TL_XL-1010RGBC-WS2812B, F.Cu at (164.5, 194.1)
- added U265: XL-1010RGBC, easyeda2kicad:LED-SMD_4P-L1.0-W1.0-TL_XL-1010RGBC-WS2812B, F.Cu at (175.2, 191.6)
- added U266: XL-1010RGBC, easyeda2kicad:LED-SMD_4P-L1.0-W1.0-TL_XL-1010RGBC-WS2812B, F.Cu at (181.5, 197.5)
- added U27: XL-1010RGBC, easyeda2kicad:LED-SMD_4P-L1.0-W1.0-TL_XL-1010RGBC-WS2812B, F.Cu at (123.9, 36.1)
- added U28: XL-1010RGBC, easyeda2kicad:LED-SMD_4P-L1.0-W1.0-TL_XL-1010RGBC-WS2812B, F.Cu at (130.4, 30.5)
- added U29: XL-1010RGBC, easyeda2kicad:LED-SMD_4P-L1.0-W1.0-TL_XL-1010RGBC-WS2812B, F.Cu at (138.0, 33.3)
- added U3: XL-1010RGBC, easyeda2kicad:LED-SMD_4P-L1.0-W1.0-TL_XL-1010RGBC-WS2812B, F.Cu at (72.6, 29.0)
- added U30: XL-1010RGBC, easyeda2kicad:LED-SMD_4P-L1.0-W1.0-TL_XL-1010RGBC-WS2812B, F.Cu at (152.5, 34.3)
- added U31: XL-1010RGBC, easyeda2kicad:LED-SMD_4P-L1.0-W1.0-TL_XL-1010RGBC-WS2812B, F.Cu at (155.0, 34.3)
- added U32: XL-1010RGBC, easyeda2kicad:LED-SMD_4P-L1.0-W1.0-TL_XL-1010RGBC-WS2812B, F.Cu at (159.7, 34.4)
- added U33: XL-1010RGBC, easyeda2kicad:LED-SMD_4P-L1.0-W1.0-TL_XL-1010RGBC-WS2812B, F.Cu at (155.7, 36.4)
- added U34: XL-1010RGBC, easyeda2kicad:LED-SMD_4P-L1.0-W1.0-TL_XL-1010RGBC-WS2812B, F.Cu at (166.8, 33.8)
- added U35: XL-1010RGBC, easyeda2kicad:LED-SMD_4P-L1.0-W1.0-TL_XL-1010RGBC-WS2812B, F.Cu at (177.0, 31.1)
- added U36: XL-1010RGBC, easyeda2kicad:LED-SMD_4P-L1.0-W1.0-TL_XL-1010RGBC-WS2812B, F.Cu at (166.1, 26.6)
- added U37: XL-1010RGBC, easyeda2kicad:LED-SMD_4P-L1.0-W1.0-TL_XL-1010RGBC-WS2812B, F.Cu at (163.0, 26.1)
- added U38: XL-1010RGBC, easyeda2kicad:LED-SMD_4P-L1.0-W1.0-TL_XL-1010RGBC-WS2812B, F.Cu at (180.3, 30.8)
- added U39: XL-1010RGBC, easyeda2kicad:LED-SMD_4P-L1.0-W1.0-TL_XL-1010RGBC-WS2812B, F.Cu at (181.3, 34.6)
- added U4: XL-1010RGBC, easyeda2kicad:LED-SMD_4P-L1.0-W1.0-TL_XL-1010RGBC-WS2812B, F.Cu at (71.0, 31.3)
- added U40: XL-1010RGBC, easyeda2kicad:LED-SMD_4P-L1.0-W1.0-TL_XL-1010RGBC-WS2812B, F.Cu at (181.8, 37.1)
- added U41: XL-1010RGBC, easyeda2kicad:LED-SMD_4P-L1.0-W1.0-TL_XL-1010RGBC-WS2812B, F.Cu at (183.0, 62.6)
- added U42: XL-1010RGBC, easyeda2kicad:LED-SMD_4P-L1.0-W1.0-TL_XL-1010RGBC-WS2812B, F.Cu at (180.3, 61.4)
- added U43: XL-1010RGBC, easyeda2kicad:LED-SMD_4P-L1.0-W1.0-TL_XL-1010RGBC-WS2812B, F.Cu at (177.8, 62.3)
- added U44: XL-1010RGBC, easyeda2kicad:LED-SMD_4P-L1.0-W1.0-TL_XL-1010RGBC-WS2812B, F.Cu at (177.4, 65.7)
- added U45: XL-1010RGBC, easyeda2kicad:LED-SMD_4P-L1.0-W1.0-TL_XL-1010RGBC-WS2812B, F.Cu at (180.3, 66.4)
- added U46: XL-1010RGBC, easyeda2kicad:LED-SMD_4P-L1.0-W1.0-TL_XL-1010RGBC-WS2812B, F.Cu at (180.8, 68.8)
- added U47: XL-1010RGBC, easyeda2kicad:LED-SMD_4P-L1.0-W1.0-TL_XL-1010RGBC-WS2812B, F.Cu at (184.7, 70.7)
- added U48: XL-1010RGBC, easyeda2kicad:LED-SMD_4P-L1.0-W1.0-TL_XL-1010RGBC-WS2812B, F.Cu at (189.7, 76.0)
- added U49: XL-1010RGBC, easyeda2kicad:LED-SMD_4P-L1.0-W1.0-TL_XL-1010RGBC-WS2812B, F.Cu at (194.7, 74.6)
- added U5: XL-1010RGBC, easyeda2kicad:LED-SMD_4P-L1.0-W1.0-TL_XL-1010RGBC-WS2812B, F.Cu at (68.4, 33.9)
- added U50: XL-1010RGBC, easyeda2kicad:LED-SMD_4P-L1.0-W1.0-TL_XL-1010RGBC-WS2812B, F.Cu at (197.3, 76.2)
- added U51: XL-1010RGBC, easyeda2kicad:LED-SMD_4P-L1.0-W1.0-TL_XL-1010RGBC-WS2812B, F.Cu at (206.0, 75.0)
- added U52: XL-1010RGBC, easyeda2kicad:LED-SMD_4P-L1.0-W1.0-TL_XL-1010RGBC-WS2812B, F.Cu at (201.6, 81.6)
- added U53: XL-1010RGBC, easyeda2kicad:LED-SMD_4P-L1.0-W1.0-TL_XL-1010RGBC-WS2812B, F.Cu at (191.1, 80.1)
- added U54: XL-1010RGBC, easyeda2kicad:LED-SMD_4P-L1.0-W1.0-TL_XL-1010RGBC-WS2812B, F.Cu at (188.2, 83.4)
- added U55: XL-1010RGBC, easyeda2kicad:LED-SMD_4P-L1.0-W1.0-TL_XL-1010RGBC-WS2812B, F.Cu at (180.6, 78.5)
- added U56: XL-1010RGBC, easyeda2kicad:LED-SMD_4P-L1.0-W1.0-TL_XL-1010RGBC-WS2812B, F.Cu at (155.2, 75.7)
- added U57: XL-1010RGBC, easyeda2kicad:LED-SMD_4P-L1.0-W1.0-TL_XL-1010RGBC-WS2812B, F.Cu at (153.5, 77.9)
- added U58: XL-1010RGBC, easyeda2kicad:LED-SMD_4P-L1.0-W1.0-TL_XL-1010RGBC-WS2812B, F.Cu at (148.9, 78.1)
- added U59: XL-1010RGBC, easyeda2kicad:LED-SMD_4P-L1.0-W1.0-TL_XL-1010RGBC-WS2812B, F.Cu at (146.3, 68.8)
- added U6: XL-1010RGBC, easyeda2kicad:LED-SMD_4P-L1.0-W1.0-TL_XL-1010RGBC-WS2812B, F.Cu at (64.6, 27.6)
- added U60: XL-1010RGBC, easyeda2kicad:LED-SMD_4P-L1.0-W1.0-TL_XL-1010RGBC-WS2812B, F.Cu at (137.2, 58.9)
- added U61: XL-1010RGBC, easyeda2kicad:LED-SMD_4P-L1.0-W1.0-TL_XL-1010RGBC-WS2812B, F.Cu at (137.3, 73.6)
- added U62: XL-1010RGBC, easyeda2kicad:LED-SMD_4P-L1.0-W1.0-TL_XL-1010RGBC-WS2812B, F.Cu at (142.8, 76.5)
- added U63: XL-1010RGBC, easyeda2kicad:LED-SMD_4P-L1.0-W1.0-TL_XL-1010RGBC-WS2812B, F.Cu at (146.0, 83.3)
- added U64: XL-1010RGBC, easyeda2kicad:LED-SMD_4P-L1.0-W1.0-TL_XL-1010RGBC-WS2812B, F.Cu at (141.8, 83.4)
- added U65: XL-1010RGBC, easyeda2kicad:LED-SMD_4P-L1.0-W1.0-TL_XL-1010RGBC-WS2812B, F.Cu at (140.4, 85.5)
- added U66: XL-1010RGBC, easyeda2kicad:LED-SMD_4P-L1.0-W1.0-TL_XL-1010RGBC-WS2812B, F.Cu at (138.1, 82.9)
- added U67: XL-1010RGBC, easyeda2kicad:LED-SMD_4P-L1.0-W1.0-TL_XL-1010RGBC-WS2812B, F.Cu at (113.3, 74.3)
- added U68: XL-1010RGBC, easyeda2kicad:LED-SMD_4P-L1.0-W1.0-TL_XL-1010RGBC-WS2812B, F.Cu at (104.5, 82.2)
- added U69: XL-1010RGBC, easyeda2kicad:LED-SMD_4P-L1.0-W1.0-TL_XL-1010RGBC-WS2812B, F.Cu at (101.0, 79.6)
- added U7: XL-1010RGBC, easyeda2kicad:LED-SMD_4P-L1.0-W1.0-TL_XL-1010RGBC-WS2812B, F.Cu at (60.1, 25.5)
- added U70: XL-1010RGBC, easyeda2kicad:LED-SMD_4P-L1.0-W1.0-TL_XL-1010RGBC-WS2812B, F.Cu at (98.6, 72.2)
- added U71: XL-1010RGBC, easyeda2kicad:LED-SMD_4P-L1.0-W1.0-TL_XL-1010RGBC-WS2812B, F.Cu at (89.8, 73.0)
- added U72: XL-1010RGBC, easyeda2kicad:LED-SMD_4P-L1.0-W1.0-TL_XL-1010RGBC-WS2812B, F.Cu at (83.1, 63.5)
- added U73: XL-1010RGBC, easyeda2kicad:LED-SMD_4P-L1.0-W1.0-TL_XL-1010RGBC-WS2812B, F.Cu at (65.8, 63.2)
- added U74: XL-1010RGBC, easyeda2kicad:LED-SMD_4P-L1.0-W1.0-TL_XL-1010RGBC-WS2812B, F.Cu at (63.6, 64.2)
- added U75: XL-1010RGBC, easyeda2kicad:LED-SMD_4P-L1.0-W1.0-TL_XL-1010RGBC-WS2812B, F.Cu at (51.0, 69.7)
- added U76: XL-1010RGBC, easyeda2kicad:LED-SMD_4P-L1.0-W1.0-TL_XL-1010RGBC-WS2812B, F.Cu at (51.3, 73.6)
- added U77: XL-1010RGBC, easyeda2kicad:LED-SMD_4P-L1.0-W1.0-TL_XL-1010RGBC-WS2812B, F.Cu at (40.9, 69.3)
- added U78: XL-1010RGBC, easyeda2kicad:LED-SMD_4P-L1.0-W1.0-TL_XL-1010RGBC-WS2812B, F.Cu at (38.3, 68.6)
- added U79: XL-1010RGBC, easyeda2kicad:LED-SMD_4P-L1.0-W1.0-TL_XL-1010RGBC-WS2812B, F.Cu at (39.8, 72.6)
- added U8: XL-1010RGBC, easyeda2kicad:LED-SMD_4P-L1.0-W1.0-TL_XL-1010RGBC-WS2812B, F.Cu at (69.5, 45.3)
- added U80: XL-1010RGBC, easyeda2kicad:LED-SMD_4P-L1.0-W1.0-TL_XL-1010RGBC-WS2812B, F.Cu at (42.2, 73.5)
- added U81: XL-1010RGBC, easyeda2kicad:LED-SMD_4P-L1.0-W1.0-TL_XL-1010RGBC-WS2812B, F.Cu at (44.8, 77.8)
- added U82: XL-1010RGBC, easyeda2kicad:LED-SMD_4P-L1.0-W1.0-TL_XL-1010RGBC-WS2812B, F.Cu at (55.1, 84.0)
- added U83: XL-1010RGBC, easyeda2kicad:LED-SMD_4P-L1.0-W1.0-TL_XL-1010RGBC-WS2812B, F.Cu at (56.6, 81.5)
- added U84: XL-1010RGBC, easyeda2kicad:LED-SMD_4P-L1.0-W1.0-TL_XL-1010RGBC-WS2812B, F.Cu at (64.4, 66.7)
- added U85: XL-1010RGBC, easyeda2kicad:LED-SMD_4P-L1.0-W1.0-TL_XL-1010RGBC-WS2812B, F.Cu at (43.3, 98.5)
- added U86: XL-1010RGBC, easyeda2kicad:LED-SMD_4P-L1.0-W1.0-TL_XL-1010RGBC-WS2812B, F.Cu at (41.1, 102.8)
- added U87: XL-1010RGBC, easyeda2kicad:LED-SMD_4P-L1.0-W1.0-TL_XL-1010RGBC-WS2812B, F.Cu at (39.2, 111.4)
- added U88: XL-1010RGBC, easyeda2kicad:LED-SMD_4P-L1.0-W1.0-TL_XL-1010RGBC-WS2812B, F.Cu at (33.7, 119.5)
- added U89: XL-1010RGBC, easyeda2kicad:LED-SMD_4P-L1.0-W1.0-TL_XL-1010RGBC-WS2812B, F.Cu at (29.6, 120.8)
- added U9: XL-1010RGBC, easyeda2kicad:LED-SMD_4P-L1.0-W1.0-TL_XL-1010RGBC-WS2812B, F.Cu at (72.1, 44.8)
- added U90: XL-1010RGBC, easyeda2kicad:LED-SMD_4P-L1.0-W1.0-TL_XL-1010RGBC-WS2812B, F.Cu at (27.0, 118.5)
- added U91: XL-1010RGBC, easyeda2kicad:LED-SMD_4P-L1.0-W1.0-TL_XL-1010RGBC-WS2812B, F.Cu at (22.7, 114.6)
- added U92: XL-1010RGBC, easyeda2kicad:LED-SMD_4P-L1.0-W1.0-TL_XL-1010RGBC-WS2812B, F.Cu at (21.1, 108.5)
- added U93: XL-1010RGBC, easyeda2kicad:LED-SMD_4P-L1.0-W1.0-TL_XL-1010RGBC-WS2812B, F.Cu at (18.8, 107.1)
- added U94: XL-1010RGBC, easyeda2kicad:LED-SMD_4P-L1.0-W1.0-TL_XL-1010RGBC-WS2812B, F.Cu at (12.5, 105.2)
- added U95: XL-1010RGBC, easyeda2kicad:LED-SMD_4P-L1.0-W1.0-TL_XL-1010RGBC-WS2812B, F.Cu at (13.2, 109.0)
- added U96: XL-1010RGBC, easyeda2kicad:LED-SMD_4P-L1.0-W1.0-TL_XL-1010RGBC-WS2812B, F.Cu at (16.6, 121.2)
- added U97: XL-1010RGBC, easyeda2kicad:LED-SMD_4P-L1.0-W1.0-TL_XL-1010RGBC-WS2812B, F.Cu at (14.6, 125.6)
- added U98: XL-1010RGBC, easyeda2kicad:LED-SMD_4P-L1.0-W1.0-TL_XL-1010RGBC-WS2812B, F.Cu at (18.4, 125.8)
- added U99: XL-1010RGBC, easyeda2kicad:LED-SMD_4P-L1.0-W1.0-TL_XL-1010RGBC-WS2812B, F.Cu at (18.5, 123.2)
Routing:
- net +5V: track 0.00 -> 228.0 mm
- net LED_Aquarius: track 0.00 -> 33.3 mm
- net LED_Andromeda: track 0.00 -> 26.4 mm
- net Net-(U7-DOUT): track 0.00 -> 24.4 mm
- net Net-(U16-DOUT): track 0.00 -> 18.1 mm
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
